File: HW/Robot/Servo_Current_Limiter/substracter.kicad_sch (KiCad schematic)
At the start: 6 parts, among them J14 1x1 2.54mm male, U1 LM324

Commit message: Something done.
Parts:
- added R26, R27: 10k, For_Rasterboard:R_Axial_DIN0207_L6.3mm_D2.5mm_Pinf_Horizontal, symbol Device:R
- added R28: 10k, For_Rasterboard:R_Axial_DIN0207_L6.3mm_D2.5mm_P7.62mm_Horizontal, symbol Device:R
- added R29: 10k, Resistor_THT:R_Axial_DIN0207_L6.3mm_D2.5mm_P5.08mm_Vertical, symbol Device:R
- added R30: 100k, For_Rasterboard:R_Axial_DIN0207_L6.3mm_D2.5mm_Pinf_Horizontal, symbol Device:R
- added RV5: 1k, Potentiometer_THT:Potentiometer_Piher_PT-10-V10_Vertical, symbol Device:R_Potentiometer
- R22: footprint For_Rasterboard:R_Axial_DIN0207_L6.3mm_D2.5mm_P7.62mm_Horizontal -> For_Rasterboard:R_Axial_DIN0207_L6.3mm_D2.5mm_P12.70mm_Horizontal
- R23: footprint Resistor_THT:R_Axial_DIN0207_L6.3mm_D2.5mm_P10.16mm_Horizontal -> Resistor_THT:R_Axial_DIN0207_L6.3mm_D2.5mm_P2.54mm_Vertical
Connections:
- net GND: now also R27.2, R28.1, R29.2, R30.2
- net OUT: now also R30.1
- net POS: now also RV5.2
- net at R21.2, R22.2, U1.12 (+): now also R28.2
- net at R23.1, R24.2, U1.13 (-): now also R29.1
- new net: R26.2, RV5.1
- new net: R27.1, RV5.3
- new net +5V: R26.1
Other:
- moved on the sheet: R21

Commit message: Working.
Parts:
- R48: renamed from R30; value 100k -> 1k
- renumbered R26 to R44, R27 to R45, R28 to R46, R29 to R47, RV5 to RV8
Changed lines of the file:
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@@
   (symbol (lib_id "power:+5V") (at 109.855 59.69 0) (unit 1)
     (in_bom yes) (on_board yes) (fields_autoplaced)
-    (property "Reference" "#PWR010" (id 0) (at 109.855 63.5 0)
+    (property "Reference" "#PWR041" (id 0) (at 109.855 63.5 0)
       (effects (font (size 1.27 1.27)) hide)
     )
@@
   (symbol (lib_id "power:GND") (at 132.08 69.215 270) (unit 1)
     (in_bom yes) (on_board yes) (fields_autoplaced)
-    (property "Reference" "#PWR020" (id 0) (at 125.73 69.215 0)
+    (property "Reference" "#PWR043" (id 0) (at 125.73 69.215 0)
       (effects (font (size 1.27 1.27)) hide)
     )
@@
   (symbol (lib_id "Device:R") (at 109.855 66.04 0) (unit 1)
     (in_bom yes) (on_board yes)
-    (property "Reference" "R26" (id 0) (at 104.5972 66.04 90))
+    (property "Reference" "R44" (id 0) (at 104.5972 66.04 90))
     (property "Value" "10k" (id 1) (at 106.9086 66.04 90))
     (property "Footprint" "For_Rasterboard:R_Axial_DIN0207_L6.3mm_D2.5mm_Pinf_Horizontal" (id 2) (at 108.077 66.04 90)
@@
   (symbol (lib_id "Device:R") (at 146.05 95.25 270) (mirror x) (unit 1)
     (in_bom yes) (on_board yes)
-    (property "Reference" "R29" (id 0) (at 146.05 100.5078 90))
+    (property "Reference" "R47" (id 0) (at 146.05 100.5078 90))
     (property "Value" "10k" (id 1) (at 146.05 98.1964 90))
     (property "Footprint" "Resistor_THT:R_Axial_DIN0207_L6.3mm_D2.5mm_P5.08mm_Vertical" (id 2) (at 146.05 97.028 90)
@@
   (symbol (lib_id "Device:R_Potentiometer") (at 109.855 76.2 0) (unit 1)
     (in_bom yes) (on_board yes) (fields_autoplaced)
-    (property "Reference" "RV5" (id 0) (at 107.315 74.9299 0)
+    (property "Reference" "RV8" (id 0) (at 107.315 74.9299 0)
       (effects (font (size 1.27 1.27)) (justify right))
     )
@@
   (symbol (lib_id "power:GND") (at 132.08 95.25 270) (unit 1)
     (in_bom yes) (on_board yes) (fields_autoplaced)
-    (property "Reference" "#PWR025" (id 0) (at 125.73 95.25 0)
+    (property "Reference" "#PWR044" (id 0) (at 125.73 95.25 0)
       (effects (font (size 1.27 1.27)) hide)
     )
@@
   (symbol (lib_id "power:GND") (at 109.855 93.345 0) (mirror y) (unit 1)
     (in_bom yes) (on_board yes)
-    (property "Reference" "#PWR015" (id 0) (at 109.855 99.695 0)
+    (property "Reference" "#PWR042" (id 0) (at 109.855 99.695 0)
       (effects (font (size 1.27 1.27)) hide)
     )
@@
   (symbol (lib_id "Device:R") (at 109.855 87.63 0) (unit 1)
     (in_bom yes) (on_board yes)
-    (property "Reference" "R27" (id 0) (at 104.5972 87.63 90))
+    (property "Reference" "R45" (id 0) (at 104.5972 87.63 90))
     (property "Value" "10k" (id 1) (at 106.9086 87.63 90))
     (property "Footprint" "For_Rasterboard:R_Axial_DIN0207_L6.3mm_D2.5mm_Pinf_Horizontal" (id 2) (at 108.077 87.63 90)
@@
   (symbol (lib_id "power:GND") (at 202.565 90.17 0) (unit 1)
     (in_bom yes) (on_board yes) (fields_autoplaced)
-    (property "Reference" "#PWR030" (id 0) (at 202.565 96.52 0)
+    (property "Reference" "#PWR045" (id 0) (at 202.565 96.52 0)
       (effects (font (size 1.27 1.27)) hide)
     )
@@
   (symbol (lib_id "Device:R") (at 146.05 69.215 90) (mirror x) (unit 1)
     (in_bom yes) (on_board yes)
-    (property "Reference" "R28" (id 0) (at 146.05 63.9572 90))
+    (property "Reference" "R46" (id 0) (at 146.05 63.9572 90))
     (property "Value" "10k" (id 1) (at 146.05 66.2686 90))
     (property "Footprint" "For_Rasterboard:R_Axial_DIN0207_L6.3mm_D2.5mm_P7.62mm_Horizontal" (id 2) (at 146.05 67.437 90)
@@
   (symbol (lib_id "Device:R") (at 202.565 85.09 0) (unit 1)
     (in_bom yes) (on_board yes)
-    (property "Reference" "R30" (id 0) (at 197.3072 85.09 90))
-    (property "Value" "100k" (id 1) (at 199.6186 85.09 90))
+    (property "Reference" "R48" (id 0) (at 197.3072 85.09 90))
+    (property "Value" "1k" (id 1) (at 199.6186 85.09 90))
     (property "Footprint" "For_Rasterboard:R_Axial_DIN0207_L6.3mm_D2.5mm_Pinf_Horizontal" (id 2) (at 200.787 85.09 90)
       (effects (font (size 1.27 1.27)) hide)

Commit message: Corrections.
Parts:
- R3: renamed from R21; footprint For_Rasterboard:R_Axial_DIN0207_L6.3mm_D2.5mm_Pinf_Horizontal -> For_Rasterboard:R_Axial_DIN0207_L6.3mm_D2.5mm_P7.62mm_Horizontal
- renumbered J14 to J5, R44 to R26, R45 to R27, R46 to R28, R47 to R29, R48 to R30, R22 to R4, R23 to R5, R24 to R6, RV8 to RV5
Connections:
- net OUT: now also U1.1; no longer U1.14
- net at R28.2, R3.2, R4.2: now also U1.3 (+); no longer U1.12 (+)
- net at R29.1, R5.1, R6.2: now also U1.2 (-); no longer U1.13 (-)
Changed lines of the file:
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@@
   (symbol (lib_id "power:GND") (at 132.08 59.69 270) (unit 1)
     (in_bom yes) (on_board yes) (fields_autoplaced)
-    (property "Reference" "#PWR0104" (id 0) (at 125.73 59.69 0)
+    (property "Reference" "#PWR0101" (id 0) (at 125.73 59.69 0)
       (effects (font (size 1.27 1.27)) hide)
     )
@@
   (symbol (lib_id "power:+5V") (at 109.855 59.69 0) (unit 1)
     (in_bom yes) (on_board yes) (fields_autoplaced)
-    (property "Reference" "#PWR041" (id 0) (at 109.855 63.5 0)
+    (property "Reference" "#PWR010" (id 0) (at 109.855 63.5 0)
       (effects (font (size 1.27 1.27)) hide)
     )
@@
   (symbol (lib_id "power:GND") (at 132.08 69.215 270) (unit 1)
     (in_bom yes) (on_board yes) (fields_autoplaced)
-    (property "Reference" "#PWR043" (id 0) (at 125.73 69.215 0)
+    (property "Reference" "#PWR020" (id 0) (at 125.73 69.215 0)
       (effects (font (size 1.27 1.27)) hide)
     )
@@
   (symbol (lib_id "Device:R") (at 109.855 66.04 0) (unit 1)
     (in_bom yes) (on_board yes)
-    (property "Reference" "R44" (id 0) (at 104.5972 66.04 90))
+    (property "Reference" "R26" (id 0) (at 104.5972 66.04 90))
     (property "Value" "10k" (id 1) (at 106.9086 66.04 90))
     (property "Footprint" "For_Rasterboard:R_Axial_DIN0207_L6.3mm_D2.5mm_Pinf_Horizontal" (id 2) (at 108.077 66.04 90)
@@
   (symbol (lib_id "Connector:TestPoint") (at 207.01 78.74 0) (unit 1)
     (in_bom yes) (on_board yes)
-    (property "Reference" "J14" (id 0) (at 207.01 69.85 0))
+    (property "Reference" "J5" (id 0) (at 207.01 69.85 0))
     (property "Value" "1x1 2.54mm male" (id 1) (at 207.01 72.39 0))
     (property "Footprint" "Connector_PinHeader_2.54mm:PinHeader_1x01_P2.54mm_Vertical" (id 2) (at 207.01 78.74 0)
@@
     (pin "1")
   )
-  (symbol (lib_id "Amplifier_Operational:LM324") (at 171.45 81.28 0) (unit 4)
+  (symbol (lib_id "Amplifier_Operational:LM324") (at 171.45 81.28 0) (unit 1)
     (in_bom yes) (on_board yes) (fields_autoplaced)
     (property "Reference" "U1" (id 0) (at 171.45 70.485 0))
@@
   (symbol (lib_id "Device:R") (at 146.05 95.25 270) (mirror x) (unit 1)
     (in_bom yes) (on_board yes)
-    (property "Reference" "R47" (id 0) (at 146.05 100.5078 90))
+    (property "Reference" "R29" (id 0) (at 146.05 100.5078 90))
     (property "Value" "10k" (id 1) (at 146.05 98.1964 90))
     (property "Footprint" "Resistor_THT:R_Axial_DIN0207_L6.3mm_D2.5mm_P5.08mm_Vertical" (id 2) (at 146.05 97.028 90)
@@
   (symbol (lib_id "Device:R_Potentiometer") (at 109.855 76.2 0) (unit 1)
     (in_bom yes) (on_board yes) (fields_autoplaced)
-    (property "Reference" "RV8" (id 0) (at 107.315 74.9299 0)
+    (property "Reference" "RV5" (id 0) (at 107.315 74.9299 0)
       (effects (font (size 1.27 1.27)) (justify right))
     )
@@
   (symbol (lib_id "power:GND") (at 132.08 95.25 270) (unit 1)
     (in_bom yes) (on_board yes) (fields_autoplaced)
-    (property "Reference" "#PWR044" (id 0) (at 125.73 95.25 0)
+    (property "Reference" "#PWR025" (id 0) (at 125.73 95.25 0)
       (effects (font (size 1.27 1.27)) hide)
     )
@@
   (symbol (lib_id "power:GND") (at 109.855 93.345 0) (mirror y) (unit 1)
     (in_bom yes) (on_board yes)
-    (property "Reference" "#PWR042" (id 0) (at 109.855 99.695 0)
+    (property "Reference" "#PWR015" (id 0) (at 109.855 99.695 0)
       (effects (font (size 1.27 1.27)) hide)
     )
@@
   (symbol (lib_id "Device:R") (at 109.855 87.63 0) (unit 1)
     (in_bom yes) (on_board yes)
-    (property "Reference" "R45" (id 0) (at 104.5972 87.63 90))
+    (property "Reference" "R27" (id 0) (at 104.5972 87.63 90))
     (property "Value" "10k" (id 1) (at 106.9086 87.63 90))
     (property "Footprint" "For_Rasterboard:R_Axial_DIN0207_L6.3mm_D2.5mm_Pinf_Horizontal" (id 2) (at 108.077 87.63 90)
@@
   (symbol (lib_id "power:GND") (at 202.565 90.17 0) (unit 1)
     (in_bom yes) (on_board yes) (fields_autoplaced)
-    (property "Reference" "#PWR045" (id 0) (at 202.565 96.52 0)
+    (property "Reference" "#PWR030" (id 0) (at 202.565 96.52 0)
       (effects (font (size 1.27 1.27)) hide)
     )
@@
   (symbol (lib_id "Device:R") (at 146.05 69.215 90) (mirror x) (unit 1)
     (in_bom yes) (on_board yes)
-    (property "Reference" "R46" (id 0) (at 146.05 63.9572 90))
+    (property "Reference" "R28" (id 0) (at 146.05 63.9572 90))
     (property "Value" "10k" (id 1) (at 146.05 66.2686 90))
     (property "Footprint" "For_Rasterboard:R_Axial_DIN0207_L6.3mm_D2.5mm_P7.62mm_Horizontal" (id 2) (at 146.05 67.437 90)
@@
   (symbol (lib_id "Device:R") (at 202.565 85.09 0) (unit 1)
     (in_bom yes) (on_board yes)
-    (property "Reference" "R48" (id 0) (at 197.3072 85.09 90))
+    (property "Reference" "R30" (id 0) (at 197.3072 85.09 90))
     (property "Value" "1k" (id 1) (at 199.6186 85.09 90))
     (property "Footprint" "For_Rasterboard:R_Axial_DIN0207_L6.3mm_D2.5mm_Pinf_Horizontal" (id 2) (at 200.787 85.09 90)
@@
   (symbol (lib_id "Device:R") (at 146.05 83.82 270) (mirror x) (unit 1)
     (in_bom yes) (on_board yes)
-    (property "Reference" "R23" (id 0) (at 146.05 89.0778 90))
+    (property "Reference" "R5" (id 0) (at 146.05 89.0778 90))
     (property "Value" "10k" (id 1) (at 146.05 86.7664 90))
     (property "Footprint" "Resistor_THT:R_Axial_DIN0207_L6.3mm_D2.5mm_P2.54mm_Vertical" (id 2) (at 146.05 85.598 90)
@@
   (symbol (lib_id "Device:R") (at 167.64 99.06 270) (unit 1)
     (in_bom yes) (on_board yes)
-    (property "Reference" "R24" (id 0) (at 167.64 93.8022 90))
+    (property "Reference" "R6" (id 0) (at 167.64 93.8022 90))
     (property "Value" "100k" (id 1) (at 167.64 96.1136 90))
     (property "Footprint" "For_Rasterboard:R_Axial_DIN0207_L6.3mm_D2.5mm_P2.54mm_Vertical" (id 2) (at 167.64 97.282 90)
@@
   (symbol (lib_id "Device:R") (at 146.05 59.69 90) (mirror x) (unit 1)
     (in_bom yes) (on_board yes)
-    (property "Reference" "R21" (id 0) (at 146.05 54.4322 90))
+    (property "Reference" "R3" (id 0) (at 146.05 54.4322 90))
     (property "Value" "100k" (id 1) (at 146.05 56.7436 90))
-    (property "Footprint" "For_Rasterboard:R_Axial_DIN0207_L6.3mm_D2.5mm_Pinf_Horizontal" (id 2) (at 146.05 57.912 90)
+    (property "Footprint" "For_Rasterboard:R_Axial_DIN0207_L6.3mm_D2.5mm_P7.62mm_Horizontal" (id 2) (at 146.05 57.912 90)
       (effects (font (size 1.27 1.27)) hide)
     )
@@
   (symbol (lib_id "Device:R") (at 146.05 78.74 90) (mirror x) (unit 1)
     (in_bom yes) (on_board yes)
-    (property "Reference" "R22" (id 0) (at 146.05 73.4822 90))
+    (property "Reference" "R4" (id 0) (at 146.05 73.4822 90))
     (property "Value" "10k" (id 1) (at 146.05 75.7936 90))
     (property "Footprint" "For_Rasterboard:R_Axial_DIN0207_L6.3mm_D2.5mm_P12.70mm_Horizontal" (id 2) (at 146.05 76.962 90)

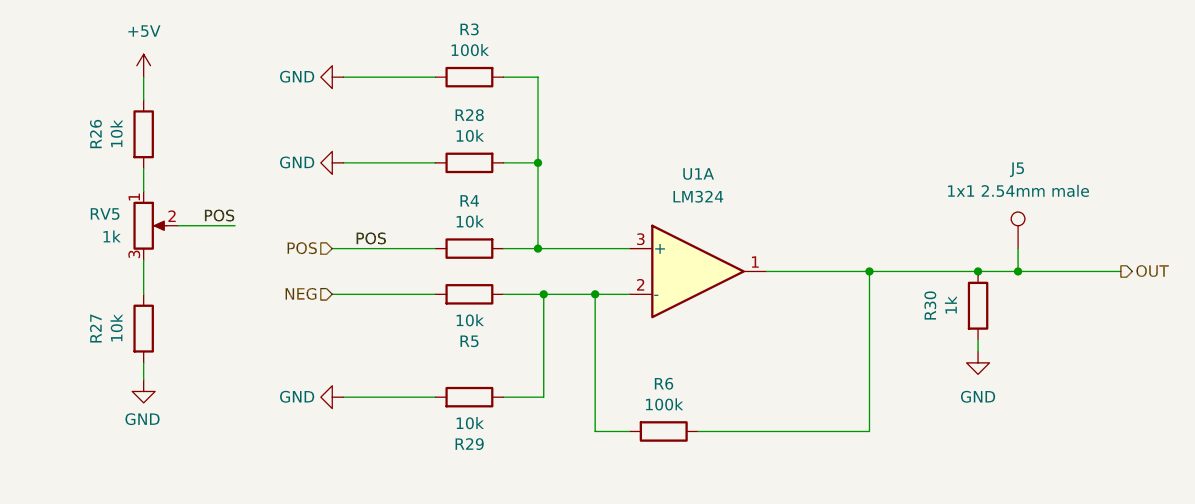
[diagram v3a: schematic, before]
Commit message: Solution for offset. Now it works.
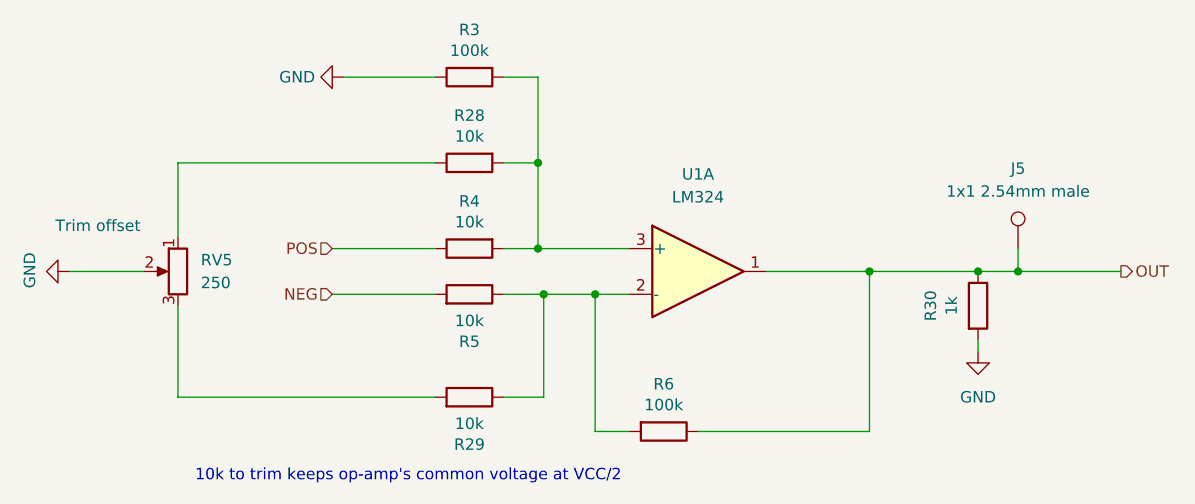
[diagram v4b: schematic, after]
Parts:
- removed R26, R27: 10k, For_Rasterboard:R_Axial_DIN0207_L6.3mm_D2.5mm_Pinf_Horizontal, symbol Device:R
- RV5: value 1k -> 250; Comment (none) -> Trim offset
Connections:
- net GND: now also RV5.2; no longer R28.1, R29.2
- net POS: no longer RV5.2
- net at RV5.1: now also R28.1
- net at RV5.3: now also R29.2
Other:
- note added: "10k to trim keeps op-amp's common voltage at VCC/2"
- moved on the sheet: RV5
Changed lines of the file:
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@@
-    (stroke (width 0) (type default) (color 0 0 0 0))
-  )
-  (wire (pts (xy 109.855 91.44) (xy 109.855 93.345))
     (stroke (width 0) (type default) (color 0 0 0 0))
   )
@@
     (stroke (width 0) (type default) (color 0 0 0 0))
   )
-  (wire (pts (xy 132.08 69.215) (xy 142.24 69.215))
+  (wire (pts (xy 113.665 69.215) (xy 142.24 69.215))
     (stroke (width 0) (type default) (color 0 0 0 0))
   )
@@
     (stroke (width 0) (type default) (color 0 0 0 0))
   )
-  (wire (pts (xy 109.855 59.69) (xy 109.855 62.23))
+  (wire (pts (xy 113.665 69.215) (xy 113.665 77.47))
     (stroke (width 0) (type default) (color 0 0 0 0))
   )
@@
     (stroke (width 0) (type default) (color 0 0 0 0))
   )
-  (wire (pts (xy 113.665 76.2) (xy 120.015 76.2))
+  (wire (pts (xy 101.6 81.28) (xy 109.855 81.28))
     (stroke (width 0) (type default) (color 0 0 0 0))
   )
@@
   )
   (wire (pts (xy 149.86 69.215) (xy 153.67 69.215))
-    (stroke (width 0) (type default) (color 0 0 0 0))
-  )
-  (wire (pts (xy 109.855 69.85) (xy 109.855 72.39))
     (stroke (width 0) (type default) (color 0 0 0 0))
   )
@@
     (stroke (width 0) (type default) (color 0 0 0 0))
   )
-  (wire (pts (xy 132.08 95.25) (xy 142.24 95.25))
+  (wire (pts (xy 113.665 95.25) (xy 142.24 95.25))
     (stroke (width 0) (type default) (color 0 0 0 0))
   )
-  (wire (pts (xy 109.855 80.01) (xy 109.855 83.82))
+  (wire (pts (xy 113.665 85.09) (xy 113.665 95.25))
     (stroke (width 0) (type default) (color 0 0 0 0))
   )
-  (label "POS" (at 120.015 76.2 180)
-    (effects (font (size 1.27 1.27)) (justify right bottom))
-  )
-  (label "POS" (at 133.35 78.74 0)
+  (text "10k to trim keeps op-amp's common voltage at VCC/2"
+    (at 115.57 104.775 0)
     (effects (font (size 1.27 1.27)) (justify left bottom))
   )
@@
     )
     (pin "1")
-  )
-  (symbol (lib_id "power:+5V") (at 109.855 59.69 0) (unit 1)
-    (in_bom yes) (on_board yes) (fields_autoplaced)
-    (property "Reference" "#PWR010" (id 0) (at 109.855 63.5 0)
-      (effects (font (size 1.27 1.27)) hide)
-    )
-    (property "Value" "+5V" (id 1) (at 109.855 54.61 0))
-    (property "Footprint" "" (id 2) (at 109.855 59.69 0)
-      (effects (font (size 1.27 1.27)) hide)
-    )
-    (property "Datasheet" "" (id 3) (at 109.855 59.69 0)
-      (effects (font (size 1.27 1.27)) hide)
-    )
-    (pin "1")
-  )
-  (symbol (lib_id "power:GND") (at 132.08 69.215 270) (unit 1)
-    (in_bom yes) (on_board yes) (fields_autoplaced)
-    (property "Reference" "#PWR020" (id 0) (at 125.73 69.215 0)
-      (effects (font (size 1.27 1.27)) hide)
-    )
-    (property "Value" "GND" (id 1) (at 128.905 69.2149 90)
-      (effects (font (size 1.27 1.27)) (justify right))
-    )
-    (property "Footprint" "" (id 2) (at 132.08 69.215 0)
-      (effects (font (size 1.27 1.27)) hide)
-    )
-    (property "Datasheet" "" (id 3) (at 132.08 69.215 0)
-      (effects (font (size 1.27 1.27)) hide)
-    )
-    (pin "1")
-  )
-  (symbol (lib_id "Device:R") (at 109.855 66.04 0) (unit 1)
-    (in_bom yes) (on_board yes)
-    (property "Reference" "R26" (id 0) (at 104.5972 66.04 90))
-    (property "Value" "10k" (id 1) (at 106.9086 66.04 90))
-    (property "Footprint" "For_Rasterboard:R_Axial_DIN0207_L6.3mm_D2.5mm_Pinf_Horizontal" (id 2) (at 108.077 66.04 90)
-      (effects (font (size 1.27 1.27)) hide)
-    )
-    (property "Datasheet" "~" (id 3) (at 109.855 66.04 0)
-      (effects (font (size 1.27 1.27)) hide)
-    )
-    (pin "1")
-    (pin "2")
   )
   (symbol (lib_id "Connector:TestPoint") (at 207.01 78.74 0) (unit 1)
@@
     (pin "2")
   )
-  (symbol (lib_id "Device:R_Potentiometer") (at 109.855 76.2 0) (unit 1)
-    (in_bom yes) (on_board yes) (fields_autoplaced)
-    (property "Reference" "RV5" (id 0) (at 107.315 74.9299 0)
+  (symbol (lib_id "Device:R_Potentiometer") (at 113.665 81.28 0) (mirror y) (unit 1)
+    (in_bom yes) (on_board yes)
+    (property "Reference" "RV5" (id 0) (at 116.205 80.0099 0)
       (effects (font (size 1.27 1.27)) (justify right))
     )
-    (property "Value" "1k" (id 1) (at 107.315 77.4699 0)
+    (property "Value" "250" (id 1) (at 116.205 82.5499 0)
       (effects (font (size 1.27 1.27)) (justify right))
     )
-    (property "Footprint" "Potentiometer_THT:Potentiometer_Piher_PT-10-V10_Vertical" (id 2) (at 109.855 76.2 0)
+    (property "Footprint" "Potentiometer_THT:Potentiometer_Piher_PT-10-V10_Vertical" (id 2) (at 113.665 81.28 0)
       (effects (font (size 1.27 1.27)) hide)
     )
-    (property "Datasheet" "~" (id 3) (at 109.855 76.2 0)
+    (property "Datasheet" "~" (id 3) (at 113.665 81.28 0)
       (effects (font (size 1.27 1.27)) hide)
     )
+    (property "Comment" "Trim offset" (id 4) (at 104.775 76.2 0))
     (pin "1")
     (pin "2")
     (pin "3")
   )
-  (symbol (lib_id "power:GND") (at 132.08 95.25 270) (unit 1)
-    (in_bom yes) (on_board yes) (fields_autoplaced)
-    (property "Reference" "#PWR025" (id 0) (at 125.73 95.25 0)
+  (symbol (lib_id "power:GND") (at 101.6 81.28 270) (mirror x) (unit 1)
+    (in_bom yes) (on_board yes)
+    (property "Reference" "#PWR015" (id 0) (at 95.25 81.28 0)
       (effects (font (size 1.27 1.27)) hide)
     )
-    (property "Value" "GND" (id 1) (at 128.905 95.2499 90)
-      (effects (font (size 1.27 1.27)) (justify right))
-    )
-    (property "Footprint" "" (id 2) (at 132.08 95.25 0)
+    (property "Value" "GND" (id 1) (at 97.2058 81.153 0))
+    (property "Footprint" "" (id 2) (at 101.6 81.28 0)
       (effects (font (size 1.27 1.27)) hide)
     )
-    (property "Datasheet" "" (id 3) (at 132.08 95.25 0)
+    (property "Datasheet" "" (id 3) (at 101.6 81.28 0)
       (effects (font (size 1.27 1.27)) hide)
     )
     (pin "1")
   )
-  (symbol (lib_id "power:GND") (at 109.855 93.345 0) (mirror y) (unit 1)
-    (in_bom yes) (on_board yes)
-    (property "Reference" "#PWR015" (id 0) (at 109.855 99.695 0)
-      (effects (font (size 1.27 1.27)) hide)
-    )
-    (property "Value" "GND" (id 1) (at 109.728 97.7392 0))
-    (property "Footprint" "" (id 2) (at 109.855 93.345 0)
-      (effects (font (size 1.27 1.27)) hide)
-    )
-    (property "Datasheet" "" (id 3) (at 109.855 93.345 0)
-      (effects (font (size 1.27 1.27)) hide)
-    )
-    (pin "1")
-  )
-  (symbol (lib_id "Device:R") (at 109.855 87.63 0) (unit 1)
-    (in_bom yes) (on_board yes)
-    (property "Reference" "R27" (id 0) (at 104.5972 87.63 90))
-    (property "Value" "10k" (id 1) (at 106.9086 87.63 90))
-    (property "Footprint" "For_Rasterboard:R_Axial_DIN0207_L6.3mm_D2.5mm_Pinf_Horizontal" (id 2) (at 108.077 87.63 90)
-      (effects (font (size 1.27 1.27)) hide)
-    )
-    (property "Datasheet" "~" (id 3) (at 109.855 87.63 0)
-      (effects (font (size 1.27 1.27)) hide)
-    )
-    (pin "1")
-    (pin "2")
-  )
   (symbol (lib_id "power:GND") (at 202.565 90.17 0) (unit 1)
